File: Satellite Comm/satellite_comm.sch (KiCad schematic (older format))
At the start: 5 parts

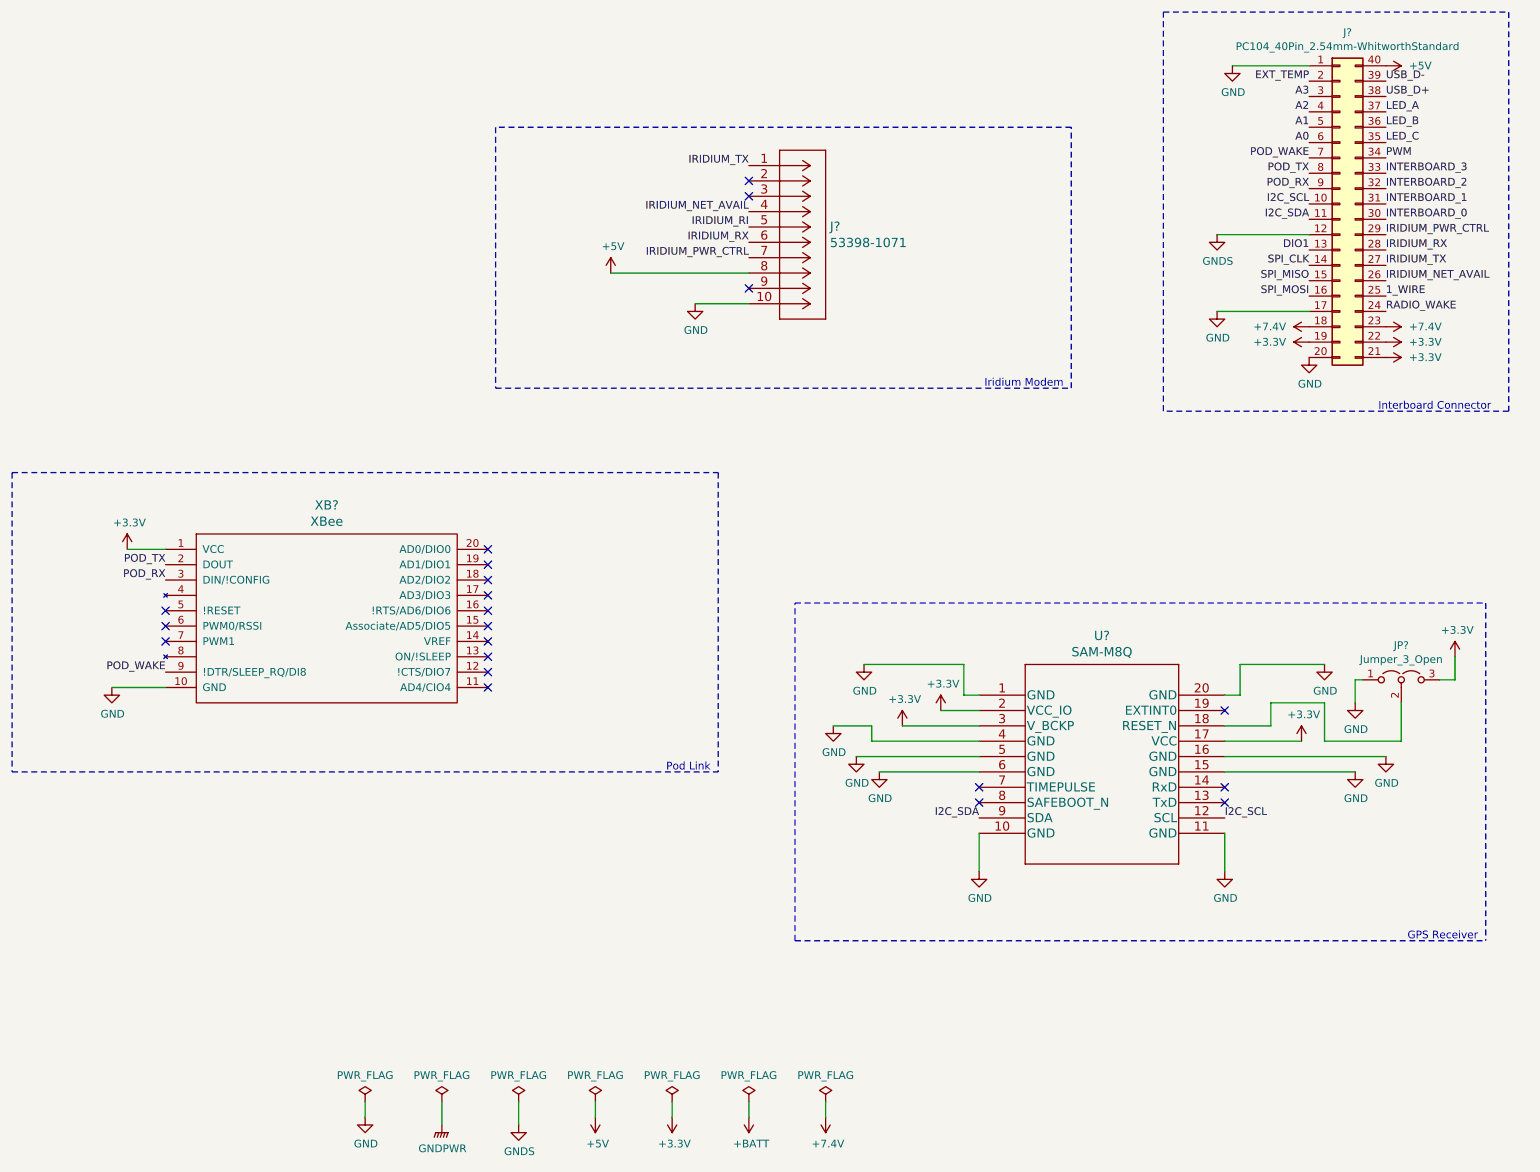
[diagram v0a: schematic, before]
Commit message: generated netlists, assigned footprints, flipped connector to rockblock
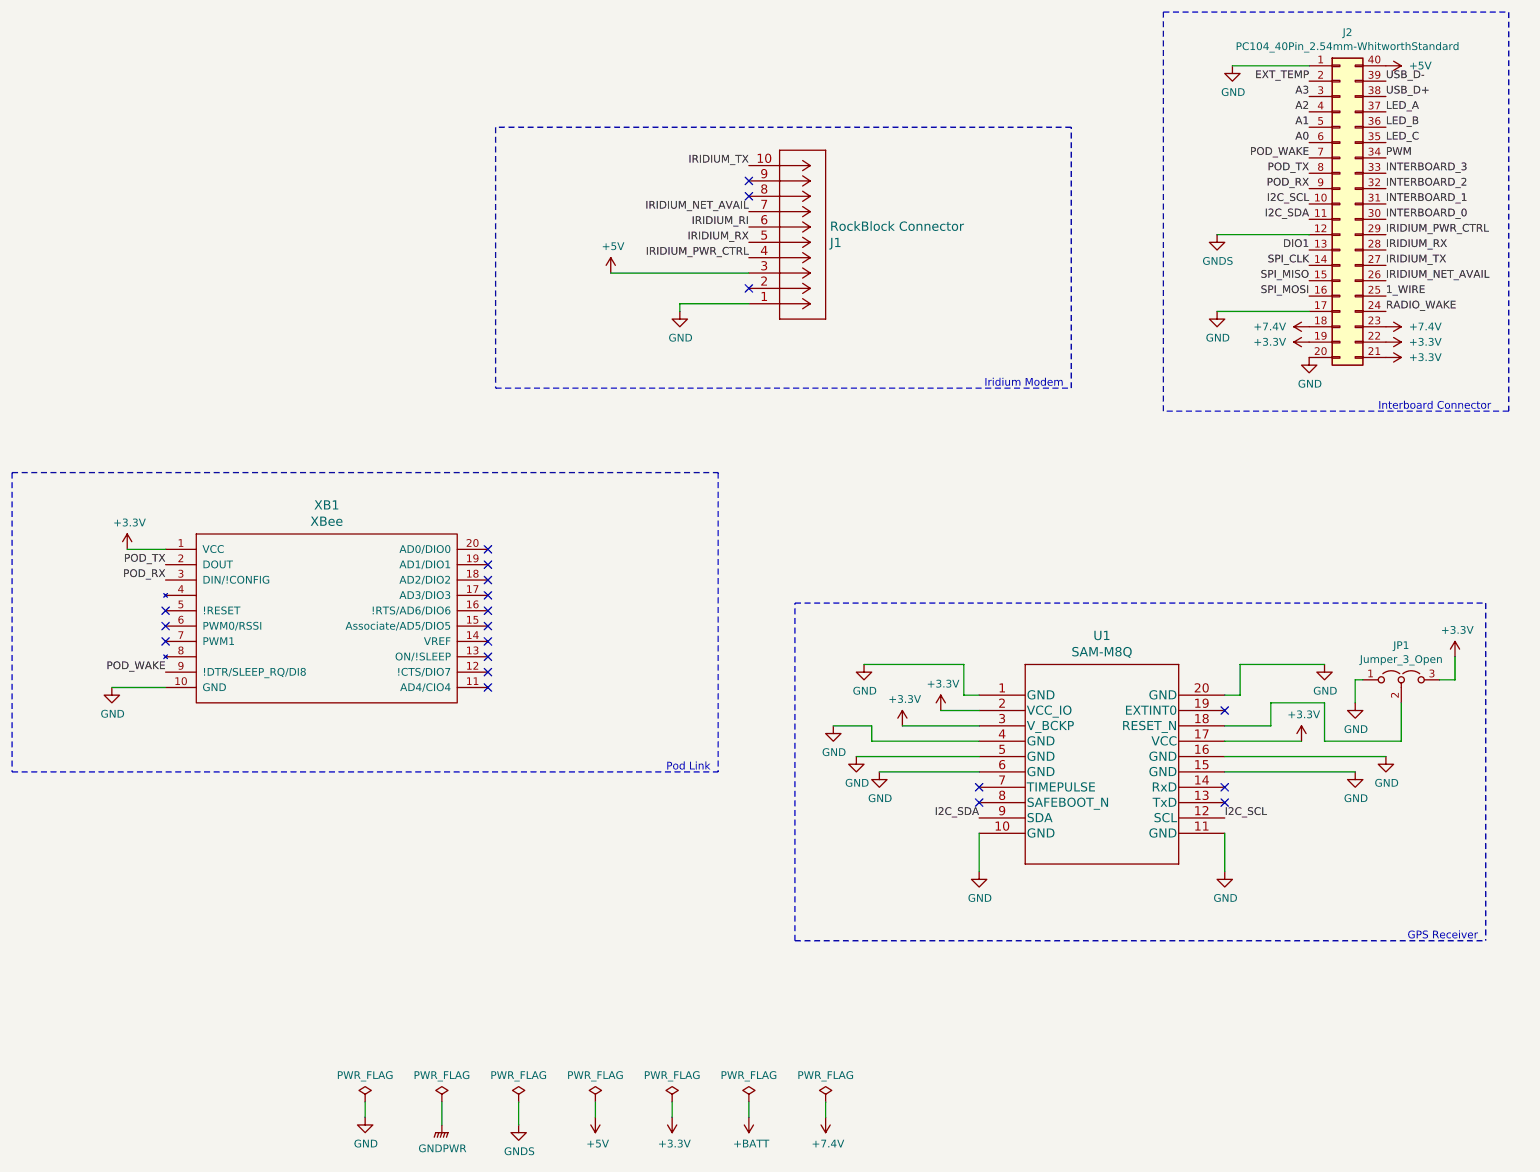
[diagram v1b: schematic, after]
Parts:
- J1: renamed from J?; value 53398-1071 -> RockBlock Connector; footprint CON00318_10 -> Connector_Molex:Molex_PicoBlade_53398-1071_1x10-1MP_P1.25mm_Vertical
- J2: renamed from J?; footprint (none) -> WhitworthStandard:PC104_40PinSocket_2.54mm
- JP1: renamed from JP?; footprint (none) -> Connector_PinHeader_2.54mm:PinHeader_1x03_P2.54mm_Vertical
- U1: renamed from U?; footprint QFN_M-M8Q -> RF_GPS:ublox_SAM-M8Q_HandSolder
- XB1: renamed from XB?; footprint (none) -> WhitworthStandard:xbee-standard
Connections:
- net +5V: now also J1.3; no longer J1.8
- net GND: now also J1.1; no longer J1.10
- net IRIDIUM_NET_AVAIL: now also J1.7; no longer J1.4
- net IRIDIUM_PWR_CTRL: now also J1.4; no longer J1.7
- net IRIDIUM_RI: now also J1.6; no longer J1.5
- net IRIDIUM_RX: now also J1.5; no longer J1.6
- net IRIDIUM_TX: now also J1.10; no longer J1.1
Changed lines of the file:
@@
 $EndComp
 $Comp
-L WhitworthStandard:PC104_40Pin_2.54mm-WhitworthStandard J?
+L WhitworthStandard:PC104_40Pin_2.54mm-WhitworthStandard J2
 U 1 1 61087887
 P 9350 1800
-F 0 "J?" H 9400 2917 50  0000 C CNN
+F 0 "J2" H 9400 2917 50  0000 C CNN
 F 1 "PC104_40Pin_2.54mm-WhitworthStandard" H 9400 2826 50  0000 C CNN
-F 2 "" H 9350 1800 50  0001 C CNN
+F 2 "WhitworthStandard:PC104_40PinSocket_2.54mm" H 9350 1800 50  0001 C CNN
 F 3 "" H 9350 1800 50  0001 C CNN
 	1    9350 1800
@@
 $EndComp
 $Comp
-L Molex_533981071:53398-1071 J?
-U 1 1 6108F4F7
-P 5900 1950
-F 0 "J?" H 6028 1953 60  0000 L CNN
-F 1 "53398-1071" H 6028 1847 60  0000 L CNN
-F 2 "CON00318_10" H 5900 1890 60  0001 C CNN
-F 3 "" H 5900 1950 60  0000 C CNN
-	1    5900 1950
-	1    0    0    -1
-$EndComp
-$Comp
-L SAM-M8Q:SAM-M8Q U?
+L SAM-M8Q:SAM-M8Q U1
 U 1 1 610913AD
 P 7000 5000
-F 0 "U?" H 7800 5387 60  0000 C CNN
+F 0 "U1" H 7800 5387 60  0000 C CNN
 F 1 "SAM-M8Q" H 7800 5281 60  0000 C CNN
-F 2 "QFN_M-M8Q" H 7800 5240 60  0001 C CNN
+F 2 "RF_GPS:ublox_SAM-M8Q_HandSolder" H 7800 5240 60  0001 C CNN
 F 3 "" H 7000 5000 60  0000 C CNN
 	1    7000 5000
@@
 IRIDIUM_TX
 $Comp
-L power:GND #PWR?
-U 1 1 610C2E58
-P 5150 2450
-F 0 "#PWR?" H 5150 2200 50  0001 C CNN
-F 1 "GND" H 5155 2277 50  0000 C CNN
-F 2 "" H 5150 2450 50  0001 C CNN
-F 3 "" H 5150 2450 50  0001 C CNN
-	1    5150 2450
-	1    0    0    -1
-$EndComp
-Wire Wire Line
-	5150 2450 5500 2450
-Text Label 5500 2050 2    50   ~ 0
-IRIDIUM_RX
-Text Label 5500 1850 2    50   ~ 0
-IRIDIUM_NET_AVAIL
-Text Label 5500 1550 2    50   ~ 0
-IRIDIUM_TX
-$Comp
-L power:+5V #PWR?
+L power:+5V #PWR0113
 U 1 1 610C5994
 P 4600 2250
-F 0 "#PWR?" H 4600 2100 50  0001 C CNN
+F 0 "#PWR0113" H 4600 2100 50  0001 C CNN
 F 1 "+5V" H 4615 2423 50  0000 C CNN
 F 2 "" H 4600 2250 50  0001 C CNN
@@
 	1    0    0    -1
 $EndComp
-Wire Wire Line
-	5500 2250 4600 2250
-$Comp
-L WhitworthStandard:XBee XB?
+$Comp
+L WhitworthStandard:XBee XB1
 U 1 1 610CDD59
 P 2750 4200
-F 0 "XB?" H 2750 4637 60  0000 C CNN
+F 0 "XB1" H 2750 4637 60  0000 C CNN
 F 1 "XBee" H 2750 4531 60  0000 C CNN
-F 2 "" H 2750 4200 60  0001 C CNN
+F 2 "WhitworthStandard:xbee-standard" H 2750 4200 60  0001 C CNN
 F 3 "" H 2750 4200 60  0001 C CNN
 	1    2750 4200
 	1    0    0    -1
 $EndComp
-Text Label 5500 1950 2    50   ~ 0
-IRIDIUM_RI
-Text Label 5500 2150 2    50   ~ 0
-IRIDIUM_PWR_CTRL
 Wire Notes Line
 	7600 1300 3850 1300
@@
 	7600 3000 7600 1300
 $Comp
-L power:GND #PWR?
+L power:GND #PWR0115
 U 1 1 610D9091
 P 6250 4800
-F 0 "#PWR?" H 6250 4550 50  0001 C CNN
+F 0 "#PWR0115" H 6250 4550 50  0001 C CNN
 F 1 "GND" H 6255 4627 50  0000 C CNN
 F 2 "" H 6250 4800 50  0001 C CNN
@@
 	6900 5000 6900 4800
 $Comp
-L power:+3.3V #PWR?
+L power:+3.3V #PWR0118
 U 1 1 610DA715
 P 6750 5100
-F 0 "#PWR?" H 6750 4950 50  0001 C CNN
+F 0 "#PWR0118" H 6750 4950 50  0001 C CNN
 F 1 "+3.3V" H 6765 5273 50  0000 C CNN
 F 2 "" H 6750 5100 50  0001 C CNN
@@
 	6250 4800 6900 4800
 $Comp
-L power:+3.3V #PWR?
+L power:+3.3V #PWR0119
 U 1 1 610DCB06
 P 6500 5200
-F 0 "#PWR?" H 6500 5050 50  0001 C CNN
+F 0 "#PWR0119" H 6500 5050 50  0001 C CNN
 F 1 "+3.3V" H 6515 5373 50  0000 C CNN
 F 2 "" H 6500 5200 50  0001 C CNN
@@
 	6500 5200 7000 5200
 $Comp
-L power:GND #PWR?
+L power:GND #PWR0120
 U 1 1 610DED48
 P 6050 5200
-F 0 "#PWR?" H 6050 4950 50  0001 C CNN
+F 0 "#PWR0120" H 6050 4950 50  0001 C CNN
 F 1 "GND" H 6055 5027 50  0000 C CNN
 F 2 "" H 6050 5200 50  0001 C CNN
@@
 $EndComp
 $Comp
-L power:GND #PWR?
+L power:GND #PWR0121
 U 1 1 610DF699
 P 6200 5400
-F 0 "#PWR?" H 6200 5150 50  0001 C CNN
+F 0 "#PWR0121" H 6200 5150 50  0001 C CNN
 F 1 "GND" H 6205 5227 50  0000 C CNN
 F 2 "" H 6200 5400 50  0001 C CNN
@@
 	6200 5400 7000 5400
 $Comp
-L power:GND #PWR?
+L power:GND #PWR0122
 U 1 1 610E4063
 P 6350 5500
-F 0 "#PWR?" H 6350 5250 50  0001 C CNN
+F 0 "#PWR0122" H 6350 5250 50  0001 C CNN
 F 1 "GND" H 6355 5327 50  0000 C CNN
 F 2 "" H 6350 5500 50  0001 C CNN
@@
 	6350 5500 7000 5500
 $Comp
-L power:GND #PWR?
+L power:GND #PWR0124
 U 1 1 610E4E40
 P 7000 6150
-F 0 "#PWR?" H 7000 5900 50  0001 C CNN
+F 0 "#PWR0124" H 7000 5900 50  0001 C CNN
 F 1 "GND" H 7005 5977 50  0000 C CNN
 F 2 "" H 7000 6150 50  0001 C CNN
@@
 	7000 5900 7000 6150
 $Comp
-L power:GND #PWR?
+L power:GND #PWR0125
 U 1 1 610E62EB
 P 8600 6150
-F 0 "#PWR?" H 8600 5900 50  0001 C CNN
+F 0 "#PWR0125" H 8600 5900 50  0001 C CNN
 F 1 "GND" H 8605 5977 50  0000 C CNN
 F 2 "" H 8600 6150 50  0001 C CNN
@@
 	8600 5900 8600 6150
 $Comp
-L power:GND #PWR?
+L power:GND #PWR0126
 U 1 1 610E6F77
 P 9250 4800
-F 0 "#PWR?" H 9250 4550 50  0001 C CNN
+F 0 "#PWR0126" H 9250 4550 50  0001 C CNN
 F 1 "GND" H 9255 4627 50  0000 C CNN
 F 2 "" H 9250 4800 50  0001 C CNN
@@
 	8700 5000 8600 5000
 $Comp
-L power:GND #PWR?
+L power:GND #PWR0127
 U 1 1 610E81D3
 P 9650 5400
-F 0 "#PWR?" H 9650 5150 50  0001 C CNN
+F 0 "#PWR0127" H 9650 5150 50  0001 C CNN
 F 1 "GND" H 9655 5227 50  0000 C CNN
 F 2 "" H 9650 5400 50  0001 C CNN
@@
 	8600 5400 9650 5400
 $Comp
-L power:GND #PWR?
+L power:GND #PWR0128
 U 1 1 610E9B44
 P 9450 5500
-F 0 "#PWR?" H 9450 5250 50  0001 C CNN
+F 0 "#PWR0128" H 9450 5250 50  0001 C CNN
 F 1 "GND" H 9455 5327 50  0000 C CNN
 F 2 "" H 9450 5500 50  0001 C CNN
@@
 	8600 5500 9450 5500
 $Comp
-L power:+3.3V #PWR?
+L power:+3.3V #PWR0129
 U 1 1 610EAAB9
 P 9100 5300
-F 0 "#PWR?" H 9100 5150 50  0001 C CNN
+F 0 "#PWR0129" H 9100 5150 50  0001 C CNN
 F 1 "+3.3V" H 9115 5473 50  0000 C CNN
 F 2 "" H 9100 5300 50  0001 C CNN
@@
 GPS Receiver
 $Comp
-L power:+3.3V #PWR?
+L power:+3.3V #PWR0130
 U 1 1 610F977C
 P 1450 4050
-F 0 "#PWR?" H 1450 3900 50  0001 C CNN
+F 0 "#PWR0130" H 1450 3900 50  0001 C CNN
 F 1 "+3.3V" H 1465 4223 50  0000 C CNN
 F 2 "" H 1450 4050 50  0001 C CNN
@@
 	1450 4050 1700 4050
 $Comp
-L power:GND #PWR?
+L power:GND #PWR0131
 U 1 1 610FAD6E
 P 1350 4950
-F 0 "#PWR?" H 1350 4700 50  0001 C CNN
+F 0 "#PWR0131" H 1350 4700 50  0001 C CNN
 F 1 "GND" H 1355 4777 50  0000 C CNN
 F 2 "" H 1350 4950 50  0001 C CNN
@@
 NoConn ~ 3800 4950
 $Comp
-L Jumper:Jumper_3_Open JP?
+L Jumper:Jumper_3_Open JP1
 U 1 1 61085CD0
 P 9750 4900
-F 0 "JP?" H 9750 5124 50  0000 C CNN
+F 0 "JP1" H 9750 5124 50  0000 C CNN
 F 1 "Jumper_3_Open" H 9750 5033 50  0000 C CNN
-F 2 "" H 9750 4900 50  0001 C CNN
+F 2 "Connector_PinHeader_2.54mm:PinHeader_1x03_P2.54mm_Vertical" H 9750 4900 50  0001 C CNN
 F 3 "~" H 9750 4900 50  0001 C CNN
 	1    9750 4900
@@
 	8900 5200 8900 5050
 $Comp
-L power:GND #PWR?
+L power:GND #PWR0132
 U 1 1 6108877D
 P 9450 5050
-F 0 "#PWR?" H 9450 4800 50  0001 C CNN
+F 0 "#PWR0132" H 9450 4800 50  0001 C CNN
 F 1 "GND" H 9455 4877 50  0000 C CNN
 F 2 "" H 9450 5050 50  0001 C CNN
@@
 	9450 4900 9450 5050
 $Comp
-L power:+3.3V #PWR?
+L power:+3.3V #PWR0133
 U 1 1 610946DF
 P 10100 4750
-F 0 "#PWR?" H 10100 4600 50  0001 C CNN
+F 0 "#PWR0133" H 10100 4600 50  0001 C CNN
 F 1 "+3.3V" H 10115 4923 50  0000 C CNN
 F 2 "" H 10100 4750 50  0001 C CNN
@@
 Wire Notes Line
 	5800 6600 10300 6600
+NoConn ~ 5500 1650
+$Comp
+L power:GND #PWR0111
+U 1 1 610C2E58
+P 5050 2500
+F 0 "#PWR0111" H 5050 2250 50  0001 C CNN
+F 1 "GND" H 5055 2327 50  0000 C CNN
+F 2 "" H 5050 2500 50  0001 C CNN
+F 3 "" H 5050 2500 50  0001 C CNN
+	1    5050 2500
+	1    0    0    -1
+$EndComp
+NoConn ~ 5500 1750
+Text Label 5500 2150 2    50   ~ 0
+IRIDIUM_PWR_CTRL
+Text Label 5500 1950 2    50   ~ 0
+IRIDIUM_RI
+Text Label 5500 1850 2    50   ~ 0
+IRIDIUM_NET_AVAIL
+Text Label 5500 2050 2    50   ~ 0
+IRIDIUM_RX
+Wire Wire Line
+	5500 2250 4600 2250
+$Comp
+L Molex_533981071:53398-1071 J1
+U 1 1 6108F4F7
+P 5900 2050
+F 0 "J1" H 6028 2053 60  0000 L CNN
+F 1 "RockBlock Connector" H 6028 1947 60  0000 L CNN
+F 2 "Connector_Molex:Molex_PicoBlade_53398-1071_1x10-1MP_P1.25mm_Vertical" H 5900 1990 60  0001 C CNN
+F 3 "" H 5900 2050 60  0000 C CNN
+	1    5900 2050
+	1    0    0    1
+$EndComp
 NoConn ~ 5500 2350
-NoConn ~ 5500 1650
-NoConn ~ 5500 1750
+Text Label 5500 1550 2    50   ~ 0
+IRIDIUM_TX
+Wire Wire Line
+	5500 2450 5050 2450
+Wire Wire Line
+	5050 2450 5050 2500
 $EndSCHEMATC

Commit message: minor, unimportant updates (deleting iridium_ri label since we aren't connecting that)
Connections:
- net IRIDIUM_RI: no longer names the net of J1.6
- no-connect marks 21 -> 23
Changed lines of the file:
@@
 Text Label 5500 2150 2    50   ~ 0
 IRIDIUM_PWR_CTRL
-Text Label 5500 1950 2    50   ~ 0
-IRIDIUM_RI
 Text Label 5500 1850 2    50   ~ 0
 IRIDIUM_NET_AVAIL
@@
 Wire Wire Line
 	5050 2450 5050 2500
+NoConn ~ 5500 1950
+NoConn ~ 1350 5800
 $EndSCHEMATC
